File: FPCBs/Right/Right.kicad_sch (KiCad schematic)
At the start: 24 parts, among them J1 PCB, J4 shutter+1st_dial, J5 2nd Focus+Shutter, J6 Conn_01x03_Pin, SW1 Mode Dial, SW2 ON/OFF, SW3 Focus+Shutter, SW4 Focus+Shutter, SW6 ON/OFF, U1 SG-105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

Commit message: Fix the buttons pins
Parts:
- removed F1: Fuse, Leica-G9ii:R_2x1mm, symbol Device:Fuse
- added R9: 5k, Leica-G9ii:R_2x1mm, symbol Device:R
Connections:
- net at J1.31 (Pin_31): now also R9.1
- net at J1.34 (Pin_34): now also RV1.2; no longer RV1.3
- net at J1.35 (Pin_35): now also RV1.3; no longer RV1.2
- net at BT1.1 (+): now also R9.2
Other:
- moved on the sheet: BT1, RV1

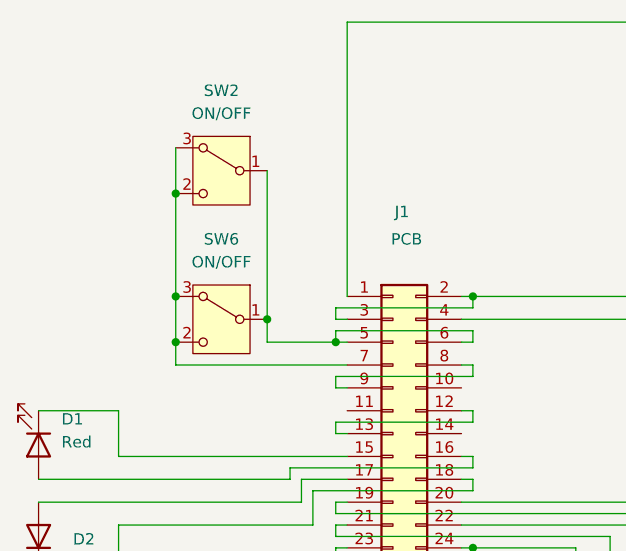
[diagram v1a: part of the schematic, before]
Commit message: Add through holes for on off switch
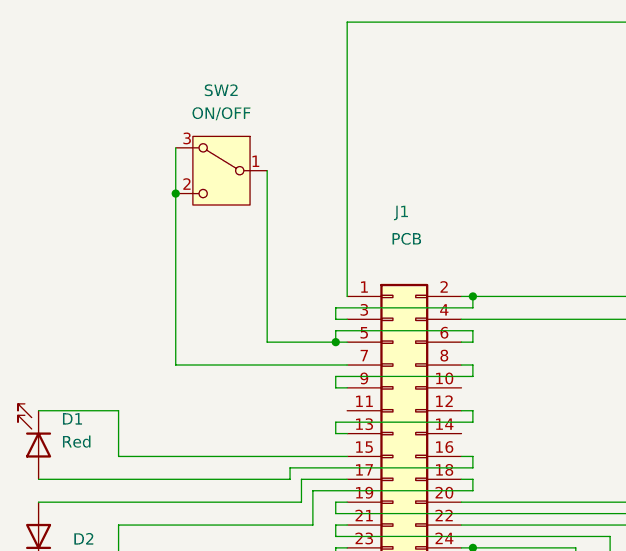
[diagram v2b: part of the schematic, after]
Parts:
- removed SW6: ON/OFF, Leica-G9ii:Switch_Detection_Bidirectional, symbol Switch:SW_SPDT_312
- SW2: footprint Leica-G9ii:Switch_Detection_Bidirectional -> Leica-G9ii:Switch_ON_OFF
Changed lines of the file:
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@@
 	)
 	(junction
-		(at 60.96 62.23)
-		(diameter 0)
-		(color 0 0 0 0)
-	)
-	(junction
-		(at 60.96 57.15)
-		(diameter 0)
-		(color 0 0 0 0)
-	)
-	(junction
 		(at 196.85 69.85)
 		(diameter 0)
@@
 	)
 	(junction
-		(at 71.12 59.69)
-		(diameter 0)
-		(color 0 0 0 0)
-	)
-	(junction
 		(at 180.34 92.71)
 		(diameter 0)
@@
 	(wire
 		(pts
-			(xy 60.96 57.15) (xy 60.96 62.23)
+			(xy 60.96 45.72) (xy 60.96 64.77)
 		)
 		(stroke
@@
 	(wire
 		(pts
-			(xy 60.96 45.72) (xy 60.96 57.15)
-		)
-		(stroke
-			(width 0)
-			(type default)
-		)
-	)
-	(wire
-		(pts
 			(xy 54.61 82.55) (xy 76.2 82.55)
 		)
@@
 	(wire
 		(pts
-			(xy 71.12 59.69) (xy 71.12 62.23)
+			(xy 71.12 43.18) (xy 71.12 62.23)
 		)
 		(stroke
@@
 	(wire
 		(pts
-			(xy 71.12 43.18) (xy 71.12 59.69)
-		)
-		(stroke
-			(width 0)
-			(type default)
-		)
-	)
-	(wire
-		(pts
 			(xy 190.5 62.23) (xy 190.5 54.61)
 		)
@@
 	(wire
 		(pts
-			(xy 60.96 62.23) (xy 60.96 64.77)
-		)
-		(stroke
-			(width 0)
-			(type default)
-		)
-	)
-	(wire
-		(pts
 			(xy 93.98 66.04) (xy 78.74 66.04)
 		)
@@
 			)
 		)
-		(property "Footprint" "Leica-G9ii:Switch_Detection_Bidirectional"
+		(property "Footprint" "Leica-G9ii:Switch_ON_OFF"
 			(at 66.04 53.34 0)
 			(effects
@@
 					(unit 1)
 				)
-			)
-		)
-	)
-	(symbol
-		(lib_id "Switch:SW_SPDT_312")
-		(at 66.04 59.69 0)
-		(mirror y)
-		(unit 1)
-		(exclude_from_sim no)
-		(in_bom yes)
-		(on_board yes)
-		(dnp no)
-		(fields_autoplaced yes)
-		(property "Reference" "SW6"
-			(at 66.04 50.8 0)
-			(effects
-				(font
-					(size 1.27 1.27)
-				)
-			)
-		)
-		(property "Value" "ON/OFF"
-			(at 66.04 53.34 0)
-			(effects
-				(font
-					(size 1.27 1.27)
-				)
-			)
-		)
-		(property "Footprint" "Leica-G9ii:Switch_Detection_Bidirectional"
-			(at 66.04 69.85 0)
-			(effects
-				(font
-					(size 1.27 1.27)
-				)
-				(hide yes)
-			)
-		)
-		(property "Datasheet" "~"
-			(at 66.04 67.31 0)
-			(effects
-				(font
-					(size 1.27 1.27)
-				)
-				(hide yes)
-			)
-		)
-		(property "Description" "Switch, single pole double throw"
-			(at 66.04 59.69 0)
-			(effects
-				(font
-					(size 1.27 1.27)
-				)
-				(hide yes)
-			)
-		)
-		(pin "3"
-		)
-		(pin "2"
-		)
-		(pin "1"
-		)
-		(instances
-			(project ""
-				(path "/4f08b7d7-0978-402f-8bca-f87716f6be32"
-					(reference "SW6")
-					(unit 1)
-				)

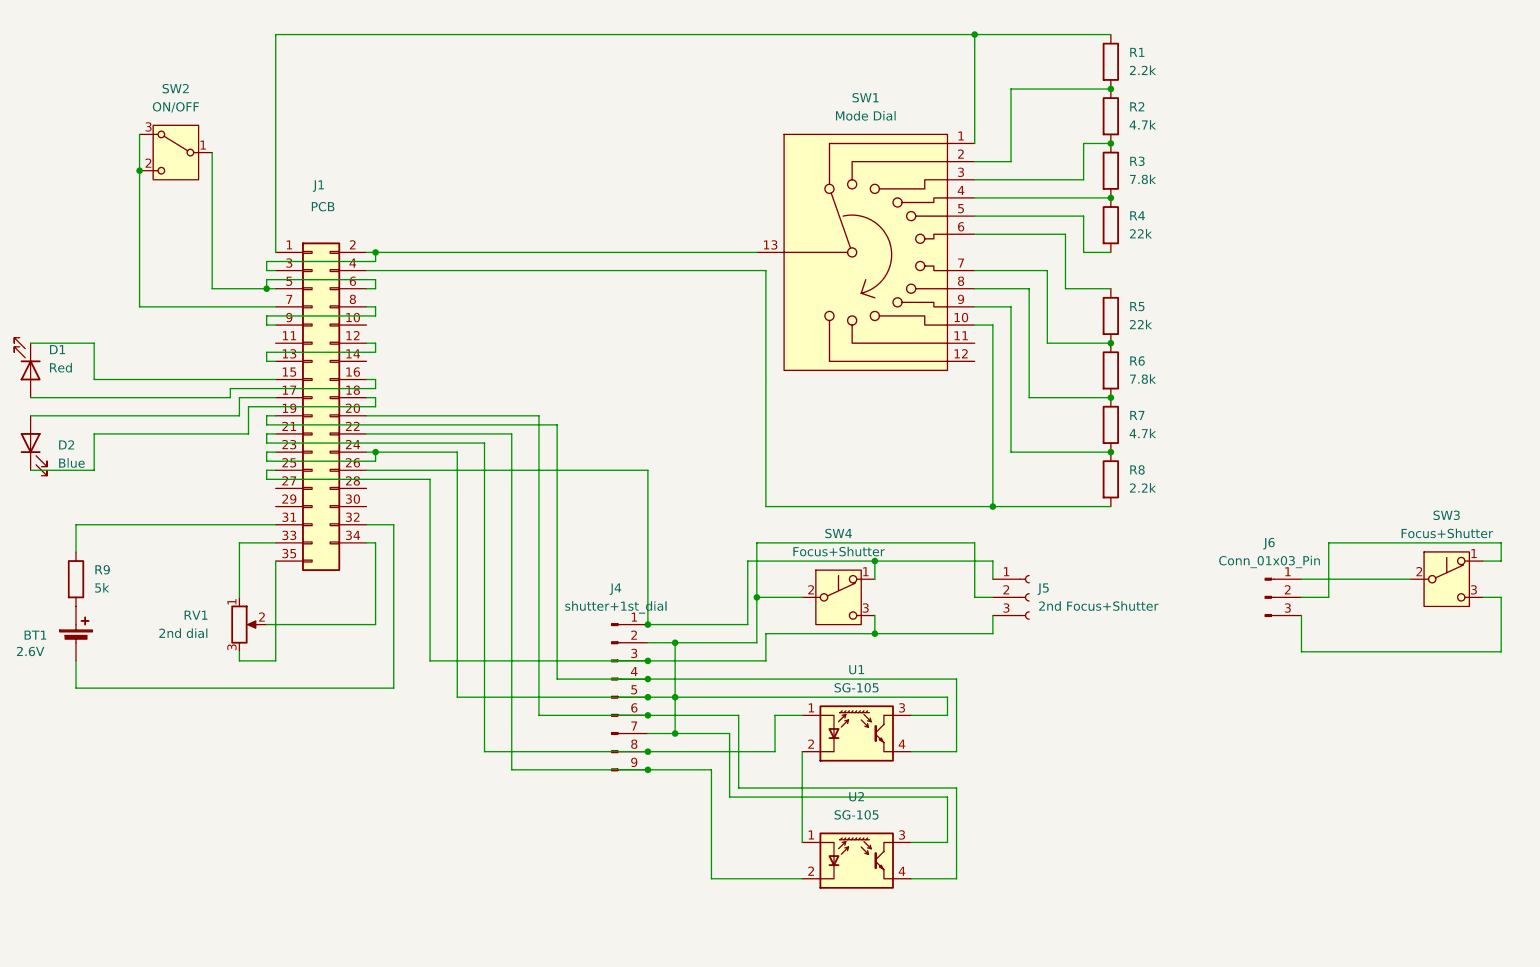
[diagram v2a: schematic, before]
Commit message: Fixes on the shutter
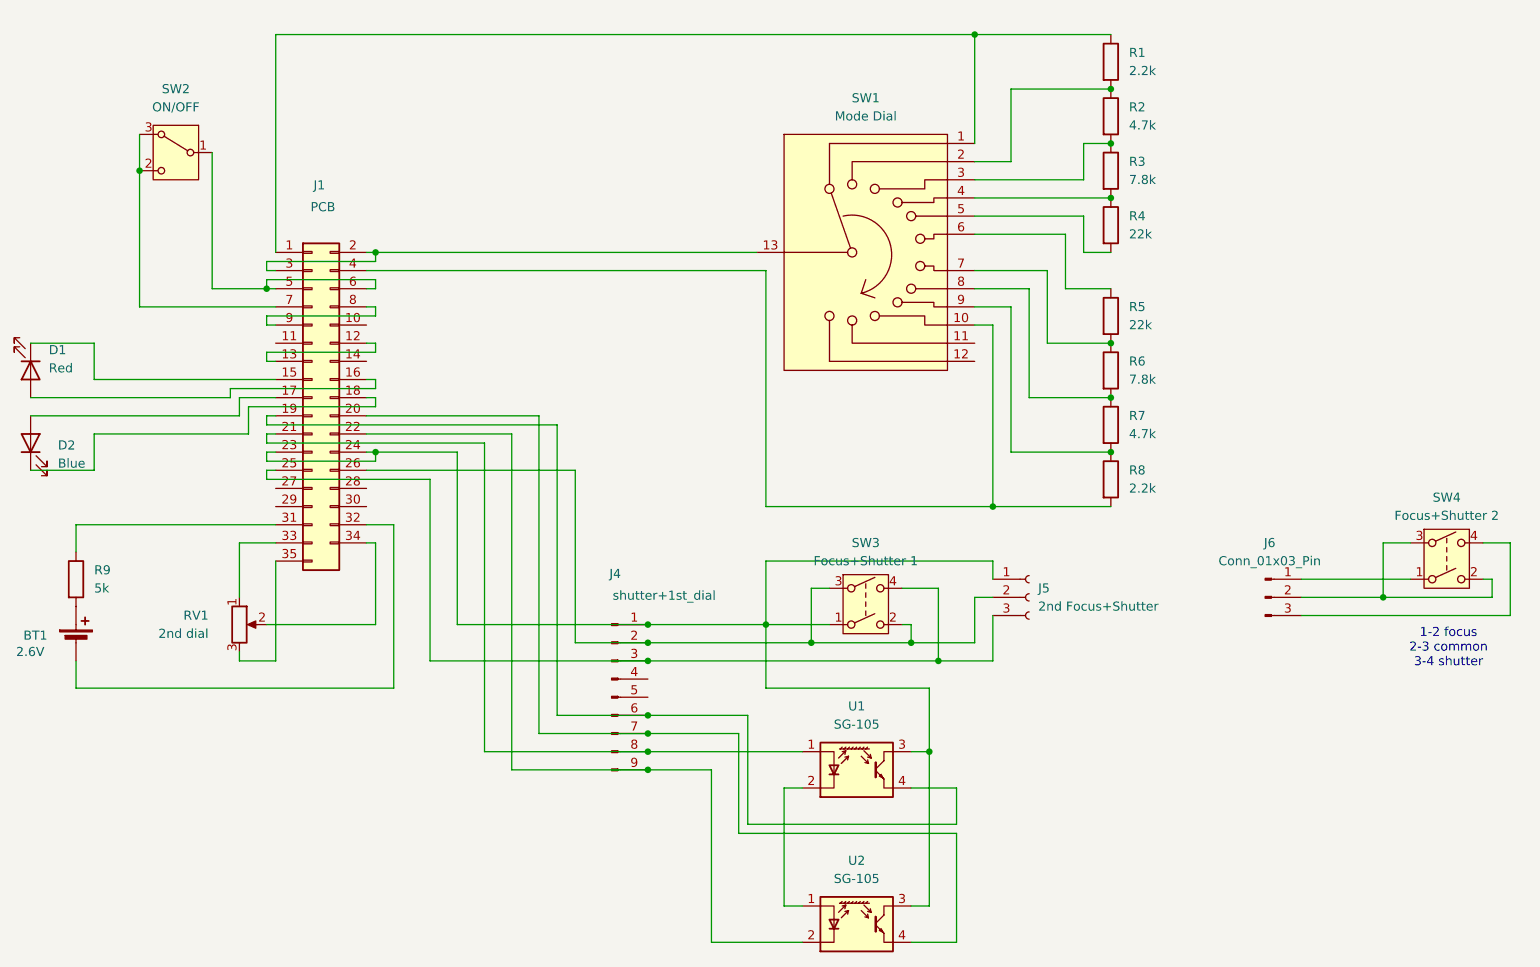
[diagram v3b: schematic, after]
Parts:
- removed SW3: Focus+Shutter, Leica-G9ii:Switch_Shutter_Olympus, symbol Switch:SW_Push_SPDT
- removed SW4: Focus+Shutter, Leica-G9ii:Switch_Shutter_Canon, symbol Switch:SW_Push_SPDT
- added SW3: Focus+Shutter 1, Leica-G9ii:Shutter_Canon, symbol Switch:SW_DPST
- added SW4: Focus+Shutter 2, Leica-G9ii:Shutter_Olympus, symbol Switch:SW_DPST
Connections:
- net at J1.19 (Pin_19), U1.4 (E): now also J4.6 (Pin_6); no longer J4.4 (Pin_4)
- net at J1.20 (Pin_20), U2.4 (E): now also J4.7 (Pin_7); no longer J4.6 (Pin_6)
- net at J1.23 (Pin_23), J1.24 (Pin_24), U1.3 (C)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: now also J4.1 (Pin_1), J5.1 (Pin_1), SW3.1; no longer J4.2 (Pin_2), J4.5 (Pin_5), J4.7 (Pin_7), J5.2 (Pin_2)
- net at J1.25 (Pin_25), J4.3 (Pin_3), J5.3 (Pin_3): now also SW3.4
- net at J6.2 (Pin_2): now also SW4.2, SW4.3
- net at J6.1 (Pin_1): now also SW4.1
- net at J6.3 (Pin_3): now also SW4.4
- new net: J1.26 (Pin_26), J4.2 (Pin_2), J5.2 (Pin_2), SW3.2, SW3.3
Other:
- note added: "1-2 focus 2-3 common 3-4 shutter"
- moved on the sheet: U1, U2

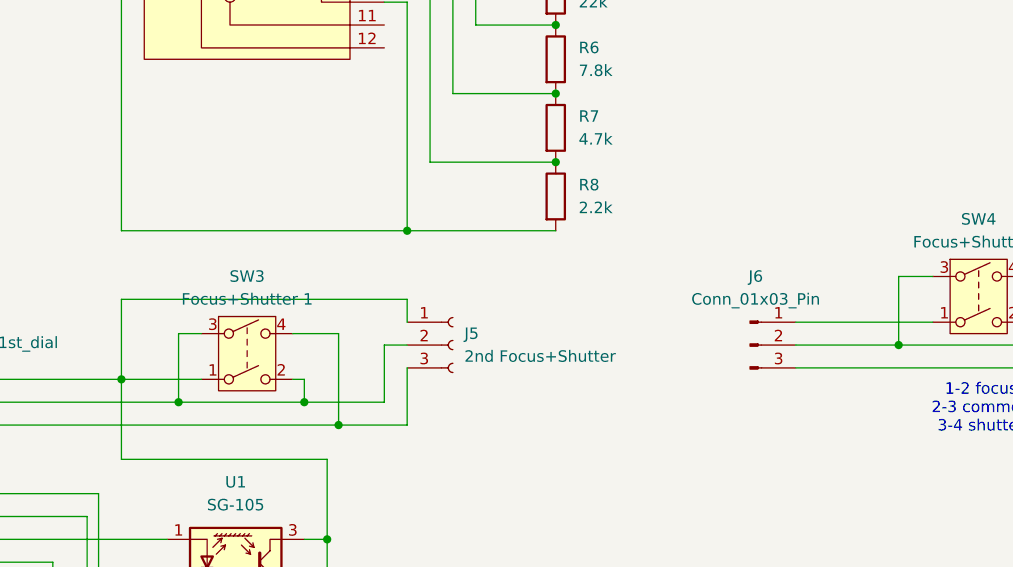
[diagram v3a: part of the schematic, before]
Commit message: Second shutter FPC
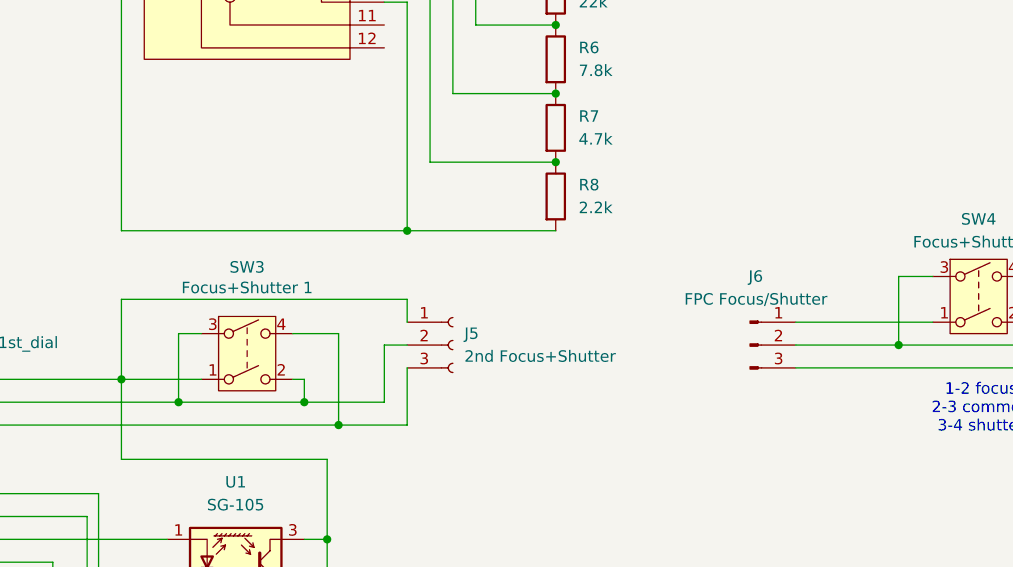
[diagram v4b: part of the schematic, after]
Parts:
- J5: footprint Leica-G9ii:Connector-4Pins -> Leica-G9ii:Connector-Springs-3Pins
- J6: value Conn_01x03_Pin -> FPC Focus/Shutter; footprint Leica-G9ii:Connector-4Pins -> Leica-G9ii:FPC-Springs-3Pins
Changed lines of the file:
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@@
 		(on_board yes)
 		(dnp no)
-		(fields_autoplaced yes)
 		(property "Reference" "SW3"
-			(at 162.56 97.79 0)
+			(at 162.56 96.774 0)
 			(effects
 				(font
@@
 		)
 		(property "Value" "Focus+Shutter 1"
-			(at 162.56 100.33 0)
+			(at 162.56 99.06 0)
 			(effects
 				(font
@@
 			)
 		)
-		(property "Footprint" "Leica-G9ii:Connector-4Pins"
+		(property "Footprint" "Leica-G9ii:Connector-Springs-3Pins"
 			(at 185.42 105.41 0)
 			(effects
@@
 			)
 		)
-		(property "Value" "Conn_01x03_Pin"
+		(property "Value" "FPC Focus/Shutter"
 			(at 219.075 100.33 0)
 			(effects
@@
 			)
 		)
-		(property "Footprint" "Leica-G9ii:Connector-4Pins"
+		(property "Footprint" "Leica-G9ii:FPC-Springs-3Pins"
 			(at 218.44 105.41 0)
 			(effects
